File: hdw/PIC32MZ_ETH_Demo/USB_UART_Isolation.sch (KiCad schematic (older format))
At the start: 8 parts

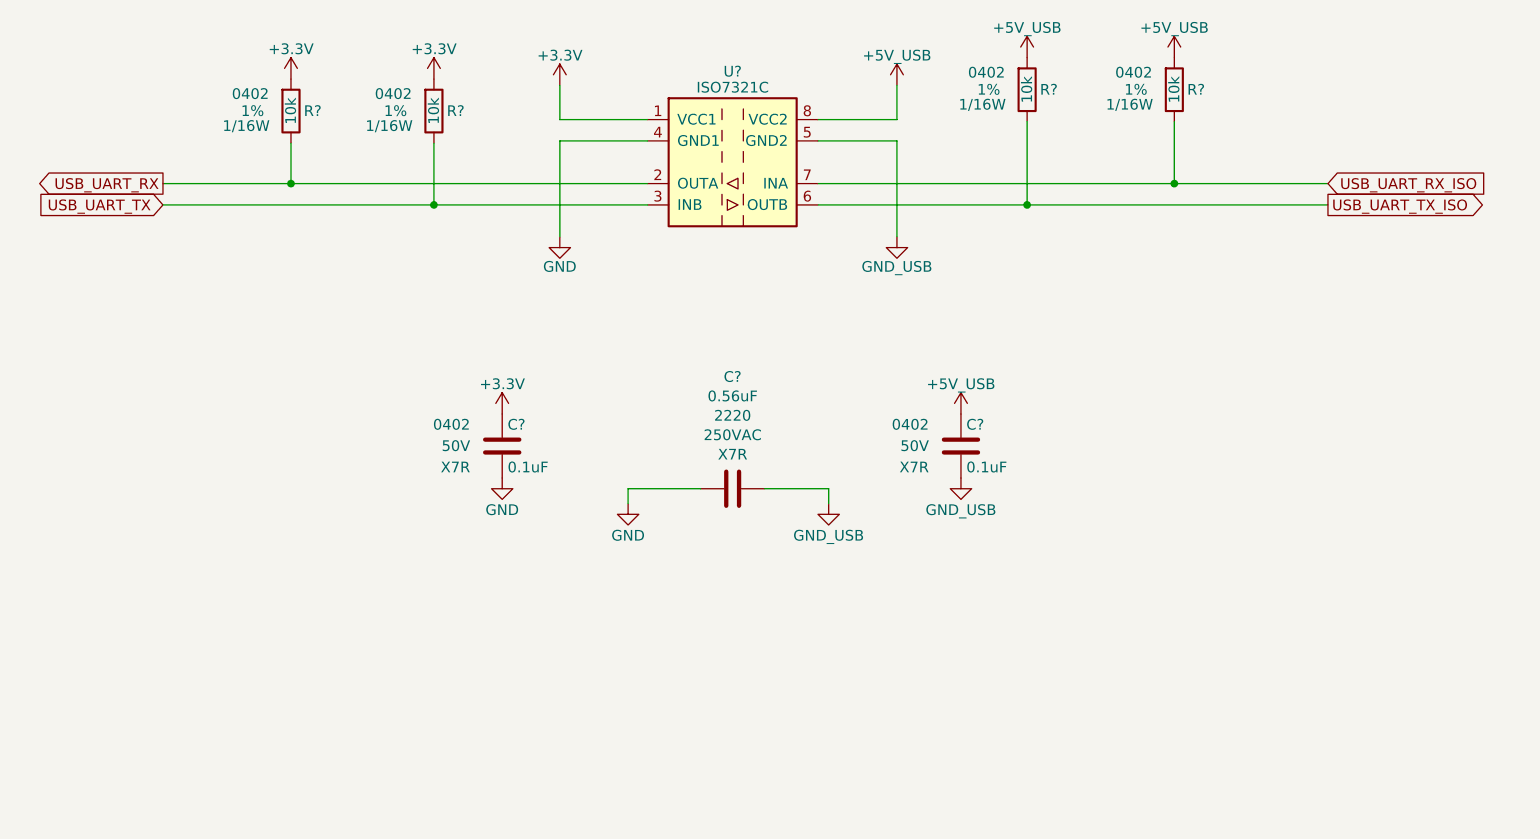
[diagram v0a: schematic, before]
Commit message: More schematic tweaks, followed PHY design guide
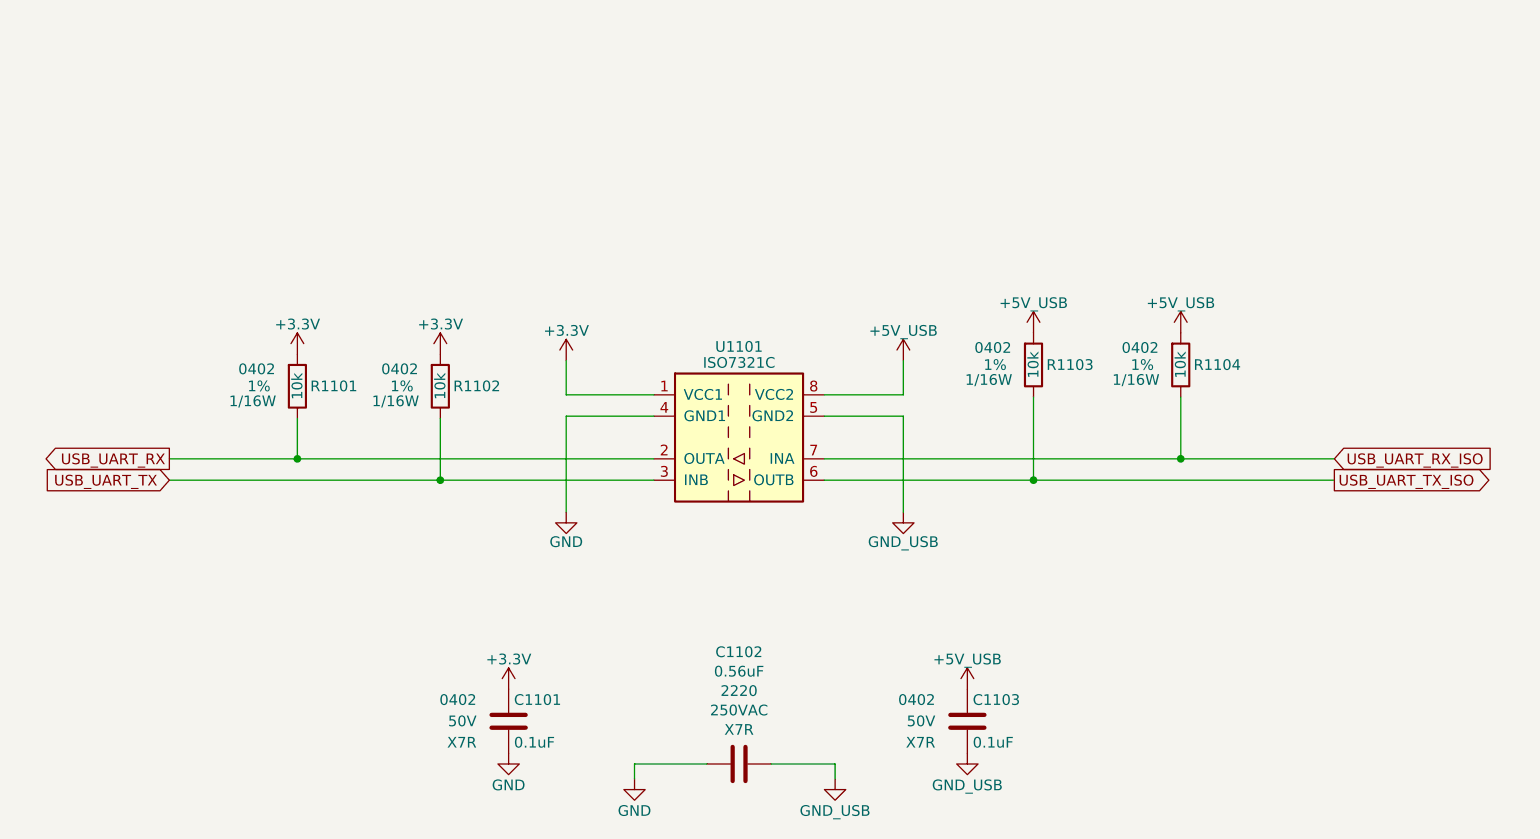
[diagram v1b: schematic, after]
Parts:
- gave numbers to parts that had none: 8
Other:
- moved on the sheet: C1101, C1102, C1103, R1101, R1102, R1103, R1104, U1101

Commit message: Populated digi-key pn's
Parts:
- C1101, C1103: Digi-Key PN (none) -> 490-10701-1-ND
- R1101, R1102, R1103, R1104: Digi-Key PN (none) -> RMCF0402FT10K0CT-ND
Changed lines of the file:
@@
 F 5 "1%" H 3640 2650 50  0000 C CNN "Tolerance"
 F 6 "1/16W" H 3670 2580 50  0000 C CNN "Wattage"
-F 7 "" H 3760 3050 60  0001 C CNN "Digi-Key PN"
+F 7 "RMCF0402FT10K0CT-ND" H 3760 3050 60  0001 C CNN "Digi-Key PN"
 	1    3460 2650
 	-1   0    0    -1
@@
 F 5 "1%" H 4310 2650 50  0000 C CNN "Tolerance"
 F 6 "1/16W" H 4340 2580 50  0000 C CNN "Wattage"
-F 7 "" H 4430 3050 60  0001 C CNN "Digi-Key PN"
+F 7 "RMCF0402FT10K0CT-ND" H 4430 3050 60  0001 C CNN "Digi-Key PN"
 	1    4130 2650
 	-1   0    0    -1
@@
 F 5 "1%" H 7090 2550 50  0000 C CNN "Tolerance"
 F 6 "1/16W" H 7120 2480 50  0000 C CNN "Wattage"
-F 7 "" H 7210 2950 60  0001 C CNN "Digi-Key PN"
+F 7 "RMCF0402FT10K0CT-ND" H 7210 2950 60  0001 C CNN "Digi-Key PN"
 	1    6910 2550
 	-1   0    0    -1
@@
 F 5 "1%" H 7780 2550 50  0000 C CNN "Tolerance"
 F 6 "1/16W" H 7810 2480 50  0000 C CNN "Wattage"
-F 7 "" H 7900 2950 60  0001 C CNN "Digi-Key PN"
+F 7 "RMCF0402FT10K0CT-ND" H 7900 2950 60  0001 C CNN "Digi-Key PN"
 	1    7600 2550
 	-1   0    0    -1
@@
 F 5 "50V" H 4300 4220 50  0000 R CNN "Voltage"
 F 6 "X7R" H 4300 4120 50  0000 R CNN "Dielectric"
-F 7 "" H 4875 4720 60  0001 C CNN "Digi-Key PN"
+F 7 "490-10701-1-ND" H 4875 4720 60  0001 C CNN "Digi-Key PN"
 	1    4450 4220
 	1    0    0    -1
@@
 F 5 "50V" H 6450 4220 50  0000 R CNN "Voltage"
 F 6 "X7R" H 6450 4120 50  0000 R CNN "Dielectric"
-F 7 "" H 7025 4720 60  0001 C CNN "Digi-Key PN"
+F 7 "490-10701-1-ND" H 7025 4720 60  0001 C CNN "Digi-Key PN"
 	1    6600 4220
 	1    0    0    -1
